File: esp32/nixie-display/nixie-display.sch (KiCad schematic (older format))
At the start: 80 parts, among them J1 Conn_01x10_Male, J2 Conn_01x10_Male, Q1 Q_NPN_CBE, Q10 Q_PNP_CBE, Q11 Q_NPN_CBE, Q12 Q_PNP_CBE, Q13 Q_NPN_CBE, Q14 Q_PNP_CBE, Q15 IRLS640, Q2 Q_PNP_CBE, Q3 Q_NPN_CBE, Q4 Q_PNP_CBE, Q5 Q_NPN_CBE, Q6 Q_PNP_CBE, Q7 Q_NPN_CBE, Q8 Q_PNP_CBE, Q9 Q_NPN_CBE, U1 MAX1771, U2 L78L05_TO92

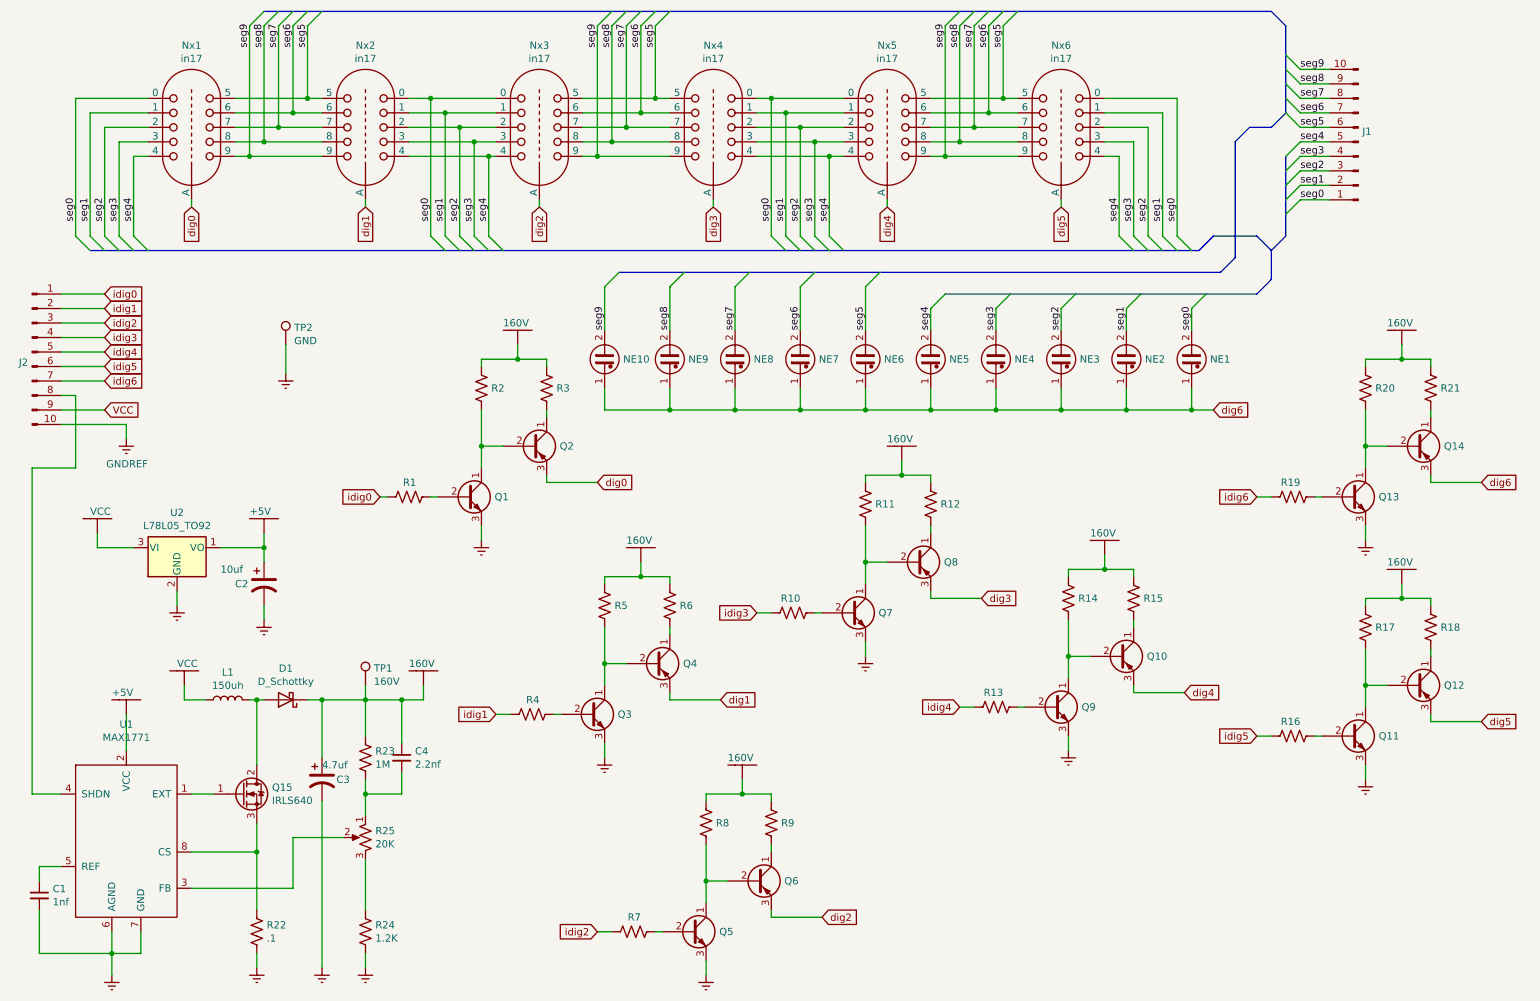
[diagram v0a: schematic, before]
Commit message: Fixed IN-17 foot prints, Anode drivers, little stuff
[git-p4: depot-paths = "//depot/nixiestat/": change = 320]
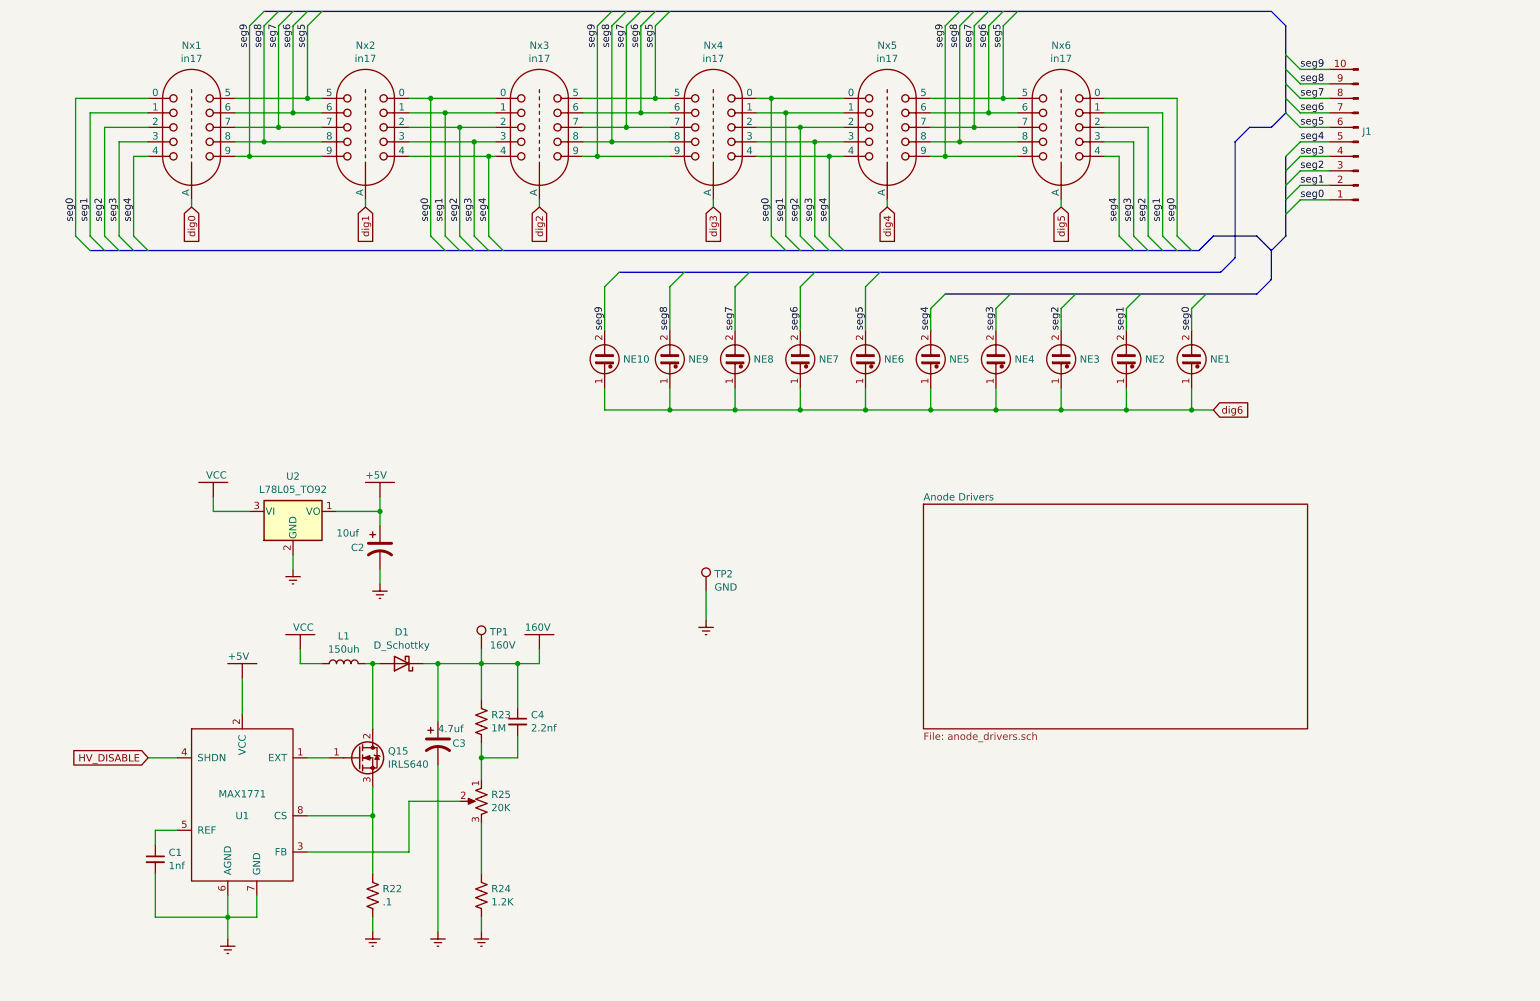
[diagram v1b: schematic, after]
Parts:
- removed J2: Conn_01x10_Male, Connector_PinHeader_2.54mm:PinHeader_1x10_P2.54mm_Vertical, symbol Connector:Conn_01x10_Male
- removed Q1, Q11, Q13, Q3, Q5, Q7, Q9: Q_NPN_CBE, Package_TO_SOT_THT:TO-92, symbol Device:Q_NPN_CBE
- removed Q10, Q12, Q14, Q2, Q4, Q6, Q8: Q_PNP_CBE, Package_TO_SOT_THT:TO-92, symbol Device:Q_PNP_CBE
- removed R1, R10, R11, R12, R13, R14, R15, R16, R17, R18, R19, R2, R20, R21, R3, R4, R5, R6, R7, R8, R9: R_US, Resistor_SMD:R_0805_2012Metric_Pad1.20x1.40mm_HandSolder, symbol Device:R_US
- removed V2, V3, V4, V5, V6, V7, V8: 160V, symbol croftj:160V
- C3: footprint Capacitor_THT:C_Radial_D6.3mm_H7.0mm_P2.50mm -> Capacitor_THT:CP_Radial_D5.0mm_P2.50mm
- NE1: value Lamp_Neon -> +2
- NE2: value Lamp_Neon -> +1
- NE3: value Lamp_Neon -> 0
- NE4: value Lamp_Neon -> -1
- NE5: value Lamp_Neon -> -2
- NE6: value Lamp_Neon -> Cool
- NE7: value Lamp_Neon -> Heat
- U2: footprint Package_TO_SOT_THT:TO-92_Inline -> Package_TO_SOT_THT:TO-92_Inline_Wide
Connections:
- net HV_DISABLE: now reaches U1.4 (SHDN)
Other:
- moved on the sheet: C1, C2, C3, C4, D1, L1, Q15, R22, R23, R24, R25, TP1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

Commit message: Improved grounding New Anode Drivers
[git-p4: depot-paths = "//depot/nixiestat/": change = 328]
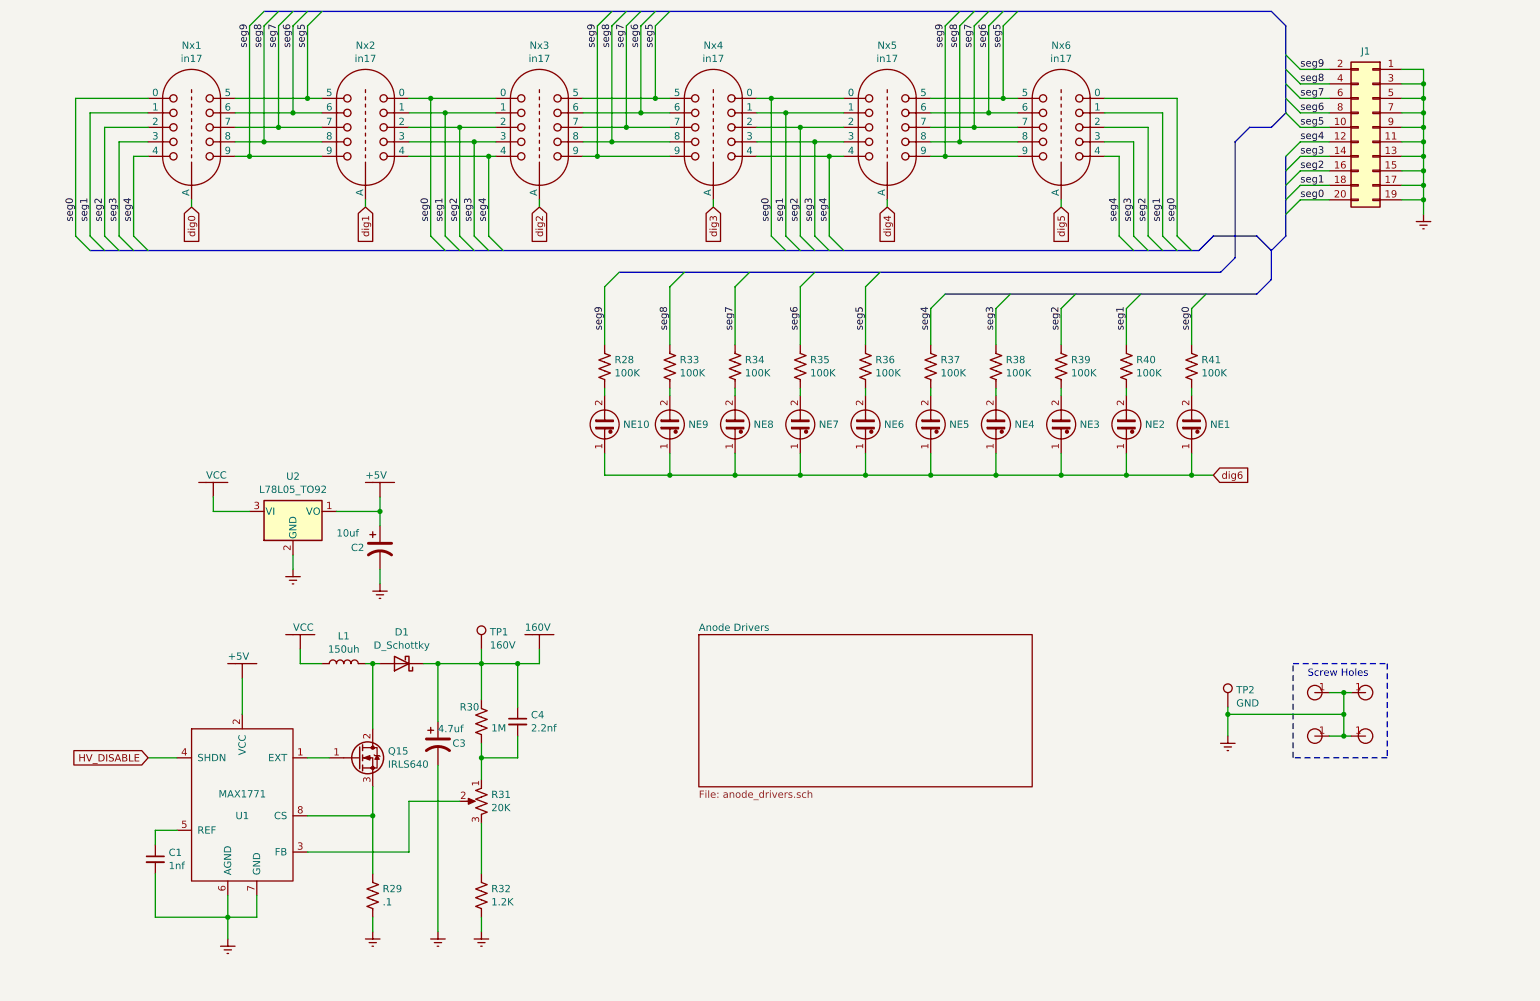
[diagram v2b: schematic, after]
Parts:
- removed J1: Conn_01x10_Male, Connector_PinHeader_2.54mm:PinHeader_1x10_P2.54mm_Vertical, symbol Connector:Conn_01x10_Male
- added J1: Conn_02x10_Odd_Even, Connector_PinHeader_2.54mm:PinHeader_2x10_P2.54mm_Vertical, symbol Connector_Generic:Conn_02x10_Odd_Even
- added R28, R33, R34, R35, R36, R37, R38, R39, R40, R41: 100K, Resistor_SMD:R_0805_2012Metric_Pad1.20x1.40mm_HandSolder, symbol Device:R_US
- added SH1, SH2, SH3, SH4: ScrewHole, croftj:4-40-Screw, symbol croftj:ScrewHole
- renumbered R22 to R29, R23 to R30, R25 to R31, R24 to R32
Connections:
- net GNDREF: now also J1.1 (Pin_1), J1.11 (Pin_11), J1.13 (Pin_13), J1.15 (Pin_15), J1.17 (Pin_17), J1.19 (Pin_19), J1.3 (Pin_3), J1.5 (Pin_5), J1.7 (Pin_7), J1.9 (Pin_9), SH1.1, SH2.1, SH3.1, SH4.1
- net seg0: now also J1.20 (Pin_20), R41.1; no longer NE1.2
- net seg1: now also J1.18 (Pin_18), R40.1; no longer NE2.2
- net seg2: now also J1.16 (Pin_16), R39.1; no longer NE3.2
- net seg3: now also J1.14 (Pin_14), R38.1; no longer NE4.2
- net seg4: now also J1.12 (Pin_12), R37.1; no longer NE5.2
- net seg5: now also J1.10 (Pin_10), R36.1; no longer NE6.2
- net seg6: now also J1.8 (Pin_8), R35.1; no longer NE7.2
- net seg7: now also J1.6 (Pin_6), R34.1; no longer NE8.2
- net seg8: now also J1.4 (Pin_4), R33.1; no longer NE9.2
- net seg9: now also J1.2 (Pin_2), R28.1; no longer NE10.2
- new net: NE1.2, R41.2
- new net: NE2.2, R40.2
- new net: NE3.2, R39.2
- new net: NE4.2, R38.2
- new net: NE5.2, R37.2
- new net: NE6.2, R36.2
- new net: NE7.2, R35.2
- new net: NE8.2, R34.2
- new net: NE9.2, R33.2
- new net: NE10.2, R28.2
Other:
- note added: "Screw Holes"
- moved on the sheet: NE1, NE10, NE2, NE3, NE4, NE5, NE6, NE7, NE8, NE9, TP2

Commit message: New Zen design
[git-p4: depot-paths = "//depot/nixiestat/": change = 356]
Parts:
- removed Nx5, Nx6: in17, croftj:in17, symbol croftj:in17
- C3: footprint Capacitor_THT:CP_Radial_D5.0mm_P2.50mm -> Capacitor_THT:CP_Radial_D8.0mm_P3.50mm
- L1: footprint Inductor_THT:L_Radial_D7.2mm_P3.00mm_MuRATA_1700 -> Inductor_THT:L_Radial_D12.5mm_P7.00mm_Fastron_09HCP
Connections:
- net dig6 is gone; now on net dig4: NE1.1, NE10.1, NE2.1, NE3.1, NE4.1, NE5.1, NE6.1, NE7.1, NE8.1, NE9.1
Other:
- moved on the sheet: Nx1, Nx2, Nx3, Nx4
